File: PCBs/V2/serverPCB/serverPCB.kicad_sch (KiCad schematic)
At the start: 7 parts, among them J2 Screw_Terminal_01x04, U4 TPSM84203

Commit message: fully updated but untested server/node code for new mini ultra boards
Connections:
- net SC_CS: now reaches MCU2.11 (D11)
- net SC_CS: now also U3.4 (L3)
- net at MCU2.A2 (A2_D14): no longer U3.4 (L3)
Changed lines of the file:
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@@
+    (stroke (width 0) (type default))
+  )
+  (wire (pts (xy 147.32 104.14) (xy 154.94 104.14))
     (stroke (width 0) (type default))
   )
@@
     (stroke (width 0) (type default))
   )
+  (wire (pts (xy 95.25 102.87) (xy 105.41 102.87))
+    (stroke (width 0) (type default))
+  )
   (wire (pts (xy 147.32 101.6) (xy 154.94 101.6))
     (stroke (width 0) (type default))
@@
   )
   (wire (pts (xy 166.37 137.16) (xy 166.37 143.51))
-    (stroke (width 0) (type default))
-  )
-  (wire (pts (xy 125.73 85.09) (xy 142.24 85.09))
     (stroke (width 0) (type default))
   )
@@
     (stroke (width 0) (type default))
   )
-  (wire (pts (xy 142.24 85.09) (xy 142.24 104.14))
-    (stroke (width 0) (type default))
-  )
   (wire (pts (xy 152.4 88.9) (xy 152.4 96.52))
-    (stroke (width 0) (type default))
-  )
-  (wire (pts (xy 154.94 104.14) (xy 142.24 104.14))
     (stroke (width 0) (type default))
   )
@@
     (effects (font (size 1.27 1.27)) (justify left bottom))
   )
+  (label "SC_CS" (at 147.32 104.14 180) (fields_autoplaced)
+    (effects (font (size 1.27 1.27)) (justify right bottom))
+  )
   (label "VBAT" (at 177.8 88.9 0) (fields_autoplaced)
     (effects (font (size 1.27 1.27)) (justify left bottom))
   )
+  (label "SC_CS" (at 95.25 102.87 180) (fields_autoplaced)
+    (effects (font (size 1.27 1.27)) (justify right bottom))
+  )
   (label "GND" (at 185.42 92.71 0) (fields_autoplaced)

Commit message: successful server integration into barebones simb program and full simb suite with dummy buffer
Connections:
- net SC_CS: now also J2.4 (Pin_4); no longer U3.4 (L3)
- net at U3.9 (H3): no longer J2.4 (Pin_4)
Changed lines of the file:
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@@
+    (stroke (width 0) (type default))
+  )
+  (wire (pts (xy 185.42 104.14) (xy 182.88 104.14))
     (stroke (width 0) (type default))
   )
@@
     (stroke (width 0) (type default))
   )
-  (wire (pts (xy 175.26 104.14) (xy 185.42 104.14))
-    (stroke (width 0) (type default))
-  )
   (wire (pts (xy 181.61 137.16) (xy 166.37 137.16))
     (stroke (width 0) (type default))
@@
   )
   (wire (pts (xy 152.4 88.9) (xy 152.4 96.52))
+    (stroke (width 0) (type default))
+  )
+  (wire (pts (xy 182.88 104.14) (xy 182.88 113.03))
     (stroke (width 0) (type default))
   )
@@
     (effects (font (size 1.27 1.27)) (justify left bottom))
   )
+  (label "SC_CS" (at 182.88 113.03 270) (fields_autoplaced)
+    (effects (font (size 1.27 1.27)) (justify right bottom))
+  )
   (label "VBAT" (at 135.89 105.41 0) (fields_autoplaced)
     (effects (font (size 1.27 1.27)) (justify left bottom))
   )
-  (label "SC_CS" (at 147.32 104.14 180) (fields_autoplaced)
-    (effects (font (size 1.27 1.27)) (justify right bottom))
-  )
   (label "VBAT" (at 177.8 88.9 0) (fields_autoplaced)

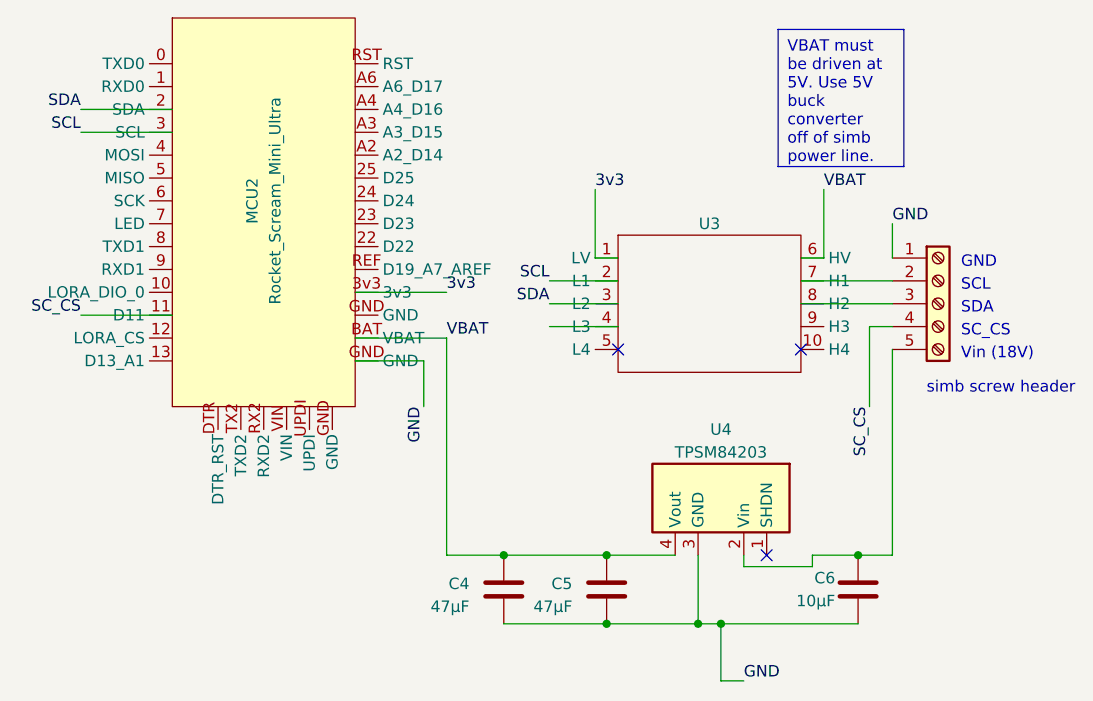
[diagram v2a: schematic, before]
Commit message: fixed pinger read error
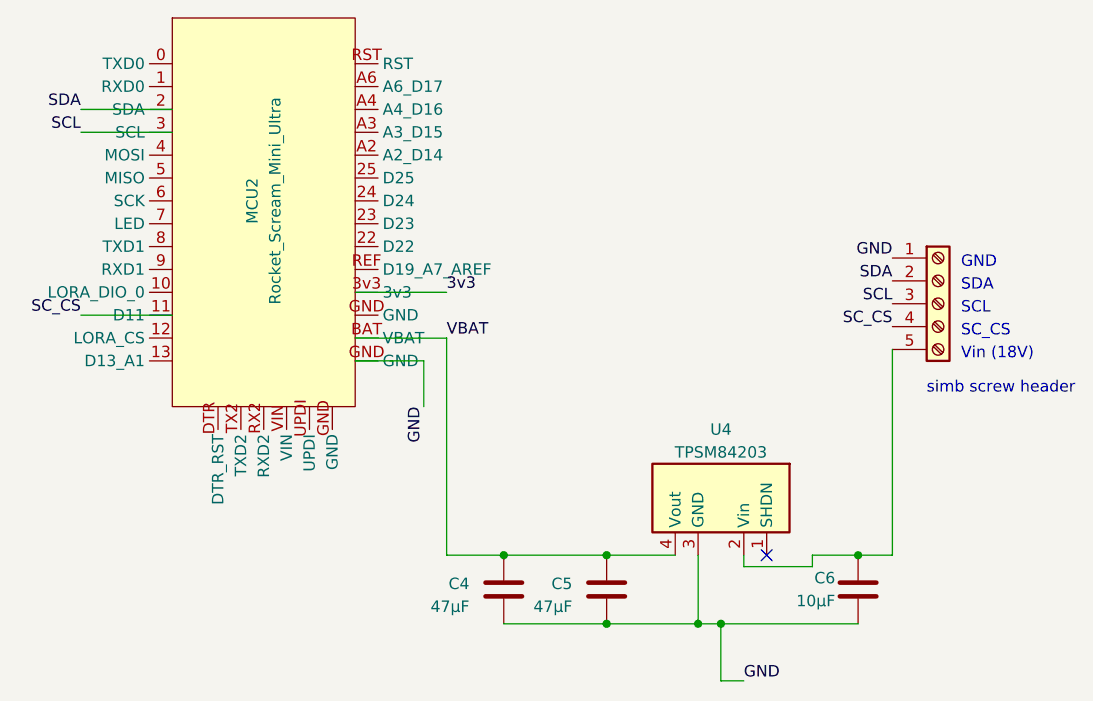
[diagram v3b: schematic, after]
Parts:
- removed U3: ~, Converter_DCDC:Pololu_logicLevelShifter, symbol Logic_LevelTranslator:Pololu_logicLevelShifter
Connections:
- net SCL: now also J2.3 (Pin_3)
- net SDA: now also J2.2 (Pin_2)
- no-connect marks 3 -> 1
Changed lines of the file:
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@@
   (junction (at 153.67 129.54) (diameter 0) (color 0 0 0 0)
   )
-  (no_connect (at 175.26 106.68))
   (no_connect (at 171.45 129.54))
-  (no_connect (at 154.94 106.68))
   (wire (pts (xy 153.67 137.16) (xy 142.24 137.16))
     (stroke (width 0) (type default))
   )
-  (wire (pts (xy 147.32 104.14) (xy 154.94 104.14))
-    (stroke (width 0) (type default))
-  )
   (wire (pts (xy 135.89 105.41) (xy 135.89 129.54))
     (stroke (width 0) (type default))
   )
-  (wire (pts (xy 154.94 96.52) (xy 152.4 96.52))
-    (stroke (width 0) (type default))
-  )
   (wire (pts (xy 168.91 130.81) (xy 176.53 130.81))
     (stroke (width 0) (type default))
@@
     (stroke (width 0) (type default))
   )
-  (wire (pts (xy 175.26 96.52) (xy 177.8 96.52))
-    (stroke (width 0) (type default))
-  )
-  (wire (pts (xy 185.42 104.14) (xy 182.88 104.14))
-    (stroke (width 0) (type default))
-  )
   (wire (pts (xy 166.37 137.16) (xy 163.83 137.16))
     (stroke (width 0) (type default))
@@
     (stroke (width 0) (type default))
   )
-  (wire (pts (xy 147.32 101.6) (xy 154.94 101.6))
-    (stroke (width 0) (type default))
-  )
   (wire (pts (xy 163.83 129.54) (xy 163.83 137.16))
     (stroke (width 0) (type default))
@@
     (stroke (width 0) (type default))
   )
-  (wire (pts (xy 177.8 88.9) (xy 177.8 96.52))
-    (stroke (width 0) (type default))
-  )
   (wire (pts (xy 153.67 129.54) (xy 142.24 129.54))
     (stroke (width 0) (type default))
@@
     (stroke (width 0) (type default))
   )
-  (wire (pts (xy 175.26 99.06) (xy 185.42 99.06))
-    (stroke (width 0) (type default))
-  )
-  (wire (pts (xy 147.32 99.06) (xy 154.94 99.06))
-    (stroke (width 0) (type default))
-  )
-  (wire (pts (xy 185.42 92.71) (xy 185.42 96.52))
-    (stroke (width 0) (type default))
-  )
-  (wire (pts (xy 175.26 101.6) (xy 185.42 101.6))
-    (stroke (width 0) (type default))
-  )
-  (wire (pts (xy 152.4 88.9) (xy 152.4 96.52))
-    (stroke (width 0) (type default))
-  )
-  (wire (pts (xy 182.88 104.14) (xy 182.88 113.03))
-    (stroke (width 0) (type default))
-  )
   (wire (pts (xy 176.53 130.81) (xy 176.53 129.54))
     (stroke (width 0) (type default))
@@
     (stroke (width 0) (type default))
   )
-  (text_box "VBAT must be driven at 5V. Use 5V buck converter off of simb power line."
-    (at 172.72 71.12 0) (size 13.97 15.24)
-    (stroke (width 0) (type default))
-    (fill (type none))
-    (effects (font (size 1.27 1.27)) (justify left top))
-  )
   (text "simb screw header" (at 205.74 111.76 0)
     (effects (font (size 1.27 1.27)) (justify right bottom))
   )
-  (text "SCL" (at 193.04 100.33 0)
+  (text "SCL" (at 193.04 102.87 0)
     (effects (font (size 1.27 1.27)) (justify left bottom))
   )
@@
     (effects (font (size 1.27 1.27)) (justify left bottom))
   )
-  (text "SDA" (at 193.04 102.87 0)
+  (text "SDA" (at 193.04 100.33 0)
     (effects (font (size 1.27 1.27)) (justify left bottom))
   )
@@
     (effects (font (size 1.27 1.27)) (justify left bottom))
   )
-  (label "SC_CS" (at 182.88 113.03 270) (fields_autoplaced)
+  (label "SCL" (at 185.42 101.6 180) (fields_autoplaced)
+    (effects (font (size 1.27 1.27)) (justify right bottom))
+  )
+  (label "SC_CS" (at 185.42 104.14 180) (fields_autoplaced)
     (effects (font (size 1.27 1.27)) (justify right bottom))
   )
@@
     (effects (font (size 1.27 1.27)) (justify left bottom))
   )
-  (label "VBAT" (at 177.8 88.9 0) (fields_autoplaced)
-    (effects (font (size 1.27 1.27)) (justify left bottom))
-  )
   (label "SC_CS" (at 95.25 102.87 180) (fields_autoplaced)
     (effects (font (size 1.27 1.27)) (justify right bottom))
   )
-  (label "GND" (at 185.42 92.71 0) (fields_autoplaced)
-    (effects (font (size 1.27 1.27)) (justify left bottom))
-  )
-  (label "3v3" (at 152.4 88.9 0) (fields_autoplaced)
-    (effects (font (size 1.27 1.27)) (justify left bottom))
-  )
-  (label "SCL" (at 147.32 99.06 180) (fields_autoplaced)
+  (label "GND" (at 185.42 96.52 180) (fields_autoplaced)
+    (effects (font (size 1.27 1.27)) (justify right bottom))
+  )
+  (label "SDA" (at 185.42 99.06 180) (fields_autoplaced)
     (effects (font (size 1.27 1.27)) (justify right bottom))
   )
@@
   )
   (label "SDA" (at 95.25 80.01 180) (fields_autoplaced)
-    (effects (font (size 1.27 1.27)) (justify right bottom))
-  )
-  (label "SDA" (at 147.32 101.6 180) (fields_autoplaced)
     (effects (font (size 1.27 1.27)) (justify right bottom))
   )
@@
         )
       )
-    )
-  )
-  (symbol (lib_id "Logic_LevelTranslator:Pololu_logicLevelShifter") (at 165.1 99.06 0) (unit 1)
-    (in_bom yes) (on_board yes) (dnp no) (fields_autoplaced)
-    (property "Reference" "U3" (at 165.1 92.71 0)
-      (effects (font (size 1.27 1.27)))
-    )
-    (property "Value" "~" (at 165.1 99.06 0)
-      (effects (font (size 1.27 1.27)))
-    )
-    (property "Footprint" "Converter_DCDC:Pololu_logicLevelShifter" (at 165.1 99.06 0)
-      (effects (font (size 1.27 1.27)) hide)
-    )
-    (property "Datasheet" "" (at 165.1 99.06 0)
-      (effects (font (size 1.27 1.27)) hide)
-    )
-    (pin "1")
-    (pin "10")
-    (pin "2")
-    (pin "3")
-    (pin "4")
-    (pin "5")
-    (pin "6")
-    (pin "7")
-    (pin "8")
-    (pin "9")
-    (instances
-      (project "serverPCB"
-        (path "/e9a5d9db-8c3f-49ab-905c-e4478fcc15ff"
-          (reference "U3") (unit 1)
-        )
-      )
